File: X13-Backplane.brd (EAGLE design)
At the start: 86.4 x 139.3 mm, 36 parts, among them J1 PXC-PTSM-04-RA-1778641, J2 PXC-PTSM-04-RA-1778641, J3 PXC-8-RA-1778683, J4 PXC-PTSM-04-RA-1778641, J5 PXC-PTSM-04-RA-1778641, J8 PXC-8-RA-1778683

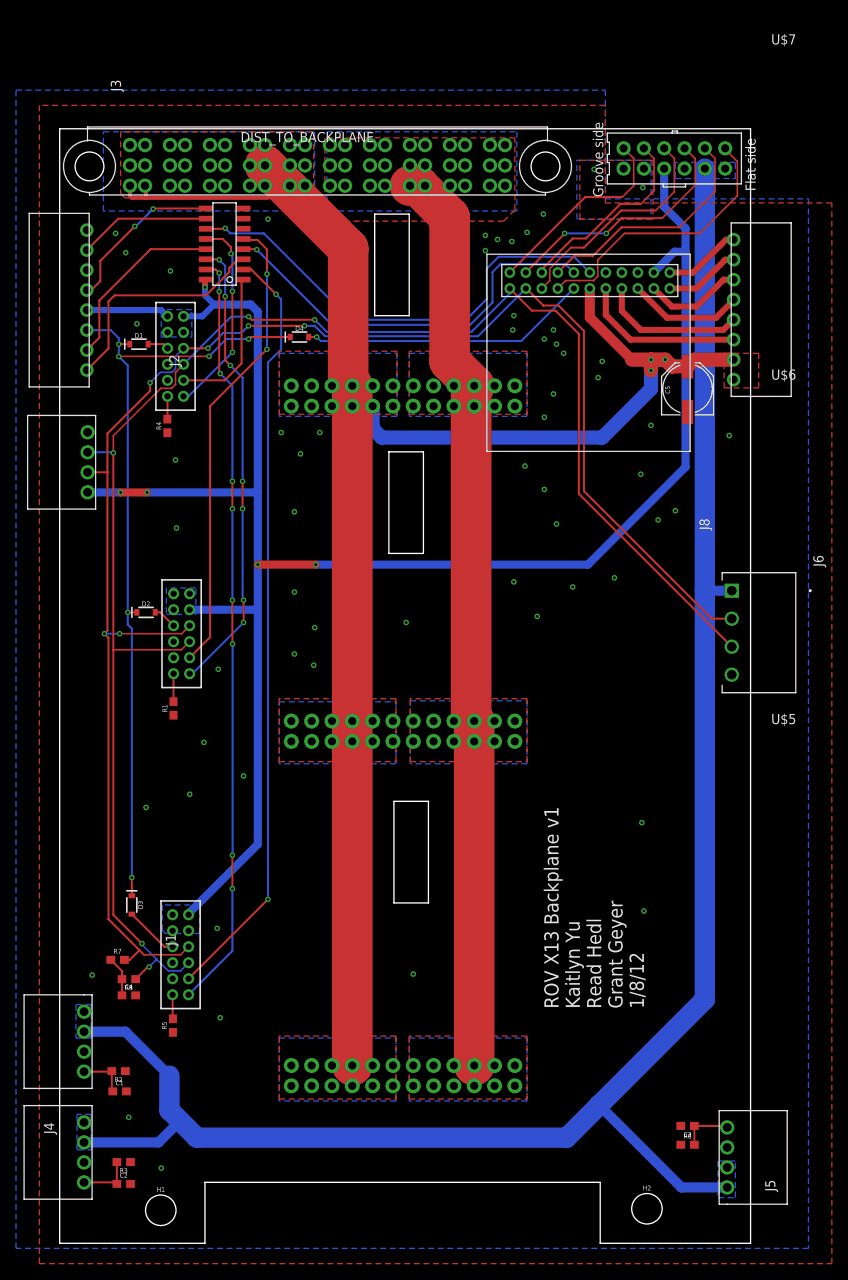
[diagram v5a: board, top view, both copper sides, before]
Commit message: OPE. GND connections were missing on esc controller connector
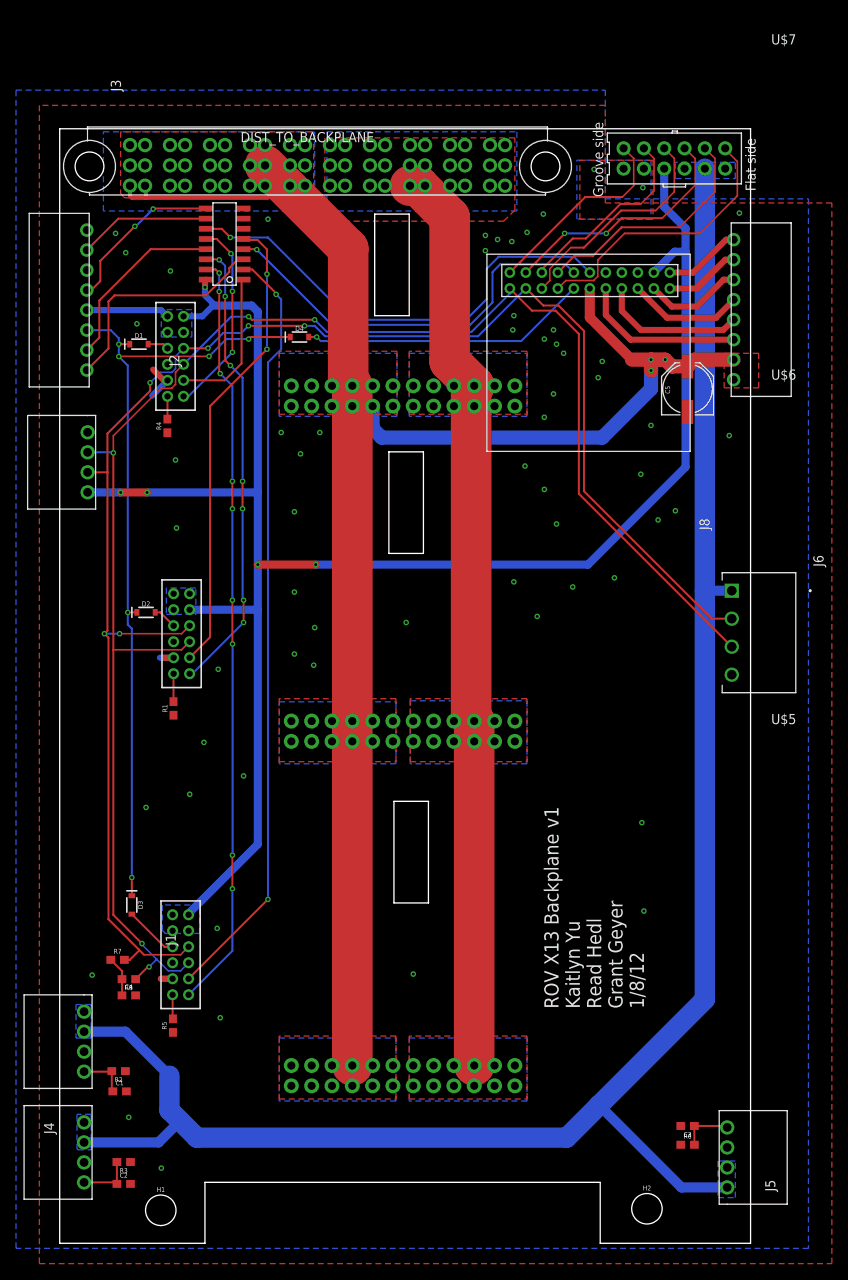
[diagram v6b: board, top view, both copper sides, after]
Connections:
- net GND: now also U$1.10, U$2.10, U$3.10
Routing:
- net GND: track 0.00 -> 10.8 mm, vias 59 -> 60
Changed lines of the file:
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@@
 <contactref element="MUX" pad="12"/>
 <contactref element="U$1" pad="11"/>
-<wire x1="25.89525" y1="125.5395" x2="28.0035" y2="125.5395" width="0.254" layer="1"/>
+<wire x1="25.89525" y1="125.5395" x2="27.2415" y2="125.5395" width="0.254" layer="1"/>
 <wire x1="29.02765" y1="123.698" x2="29.21" y2="123.51565" width="0.254" layer="16"/>
 <wire x1="29.21" y1="123.51565" x2="29.21" y2="118.999" width="0.254" layer="16"/>
@@
 <wire x1="29.21" y1="111.379" x2="23.702" y2="105.871" width="0.254" layer="16"/>
 <wire x1="23.702" y1="105.871" x2="23.098" y2="105.871" width="0.254" layer="16"/>
-<wire x1="28.0035" y1="125.5395" x2="29.02765" y2="124.51535" width="0.254" layer="1"/>
-<wire x1="29.02765" y1="124.51535" x2="29.02765" y2="123.698" width="0.254" layer="1"/>
+<wire x1="27.2415" y1="125.5395" x2="29.02765" y2="123.75335" width="0.254" layer="1"/>
+<wire x1="29.02765" y1="123.75335" x2="29.02765" y2="123.698" width="0.254" layer="1"/>
 <via x="29.02765" y="123.698" extent="1-16" drill="0.35"/>
 </signal>
@@
 <via x="39.37" y="72.263" extent="1-16" drill="0.35"/>
 <via x="30.607" y="58.42" extent="1-16" drill="0.35"/>
-<wire x1="30.57525" y1="126.8095" x2="21.463" y2="121.539" width="0" layer="19" extent="1-1"/>
+<contactref element="U$1" pad="10"/>
+<contactref element="U$2" pad="10"/>
+<contactref element="U$3" pad="10"/>
+<wire x1="21.098" y1="107.871" x2="20.653" y2="107.871" width="0.762" layer="1"/>
+<wire x1="20.653" y1="107.871" x2="19.304" y2="109.22" width="0.762" layer="1"/>
+<wire x1="21.098" y1="107.871" x2="19.177" y2="105.95" width="0.762" layer="16"/>
+<wire x1="21.86" y1="73.2" x2="20.145" y2="73.2" width="0.762" layer="16"/>
+<wire x1="21.86" y1="73.2" x2="20.622" y2="73.2" width="0.762" layer="1"/>
+<wire x1="21.733" y1="33.068" x2="20.241" y2="33.068" width="0.762" layer="1"/>
+<wire x1="21.733" y1="33.068" x2="20.399" y2="33.068" width="0.762" layer="16"/>
+<via x="92.583" y="128.778" extent="1-16" drill="0.35"/>
 </signal>
 <signal name="SWDIO_3">
 <contactref element="MUX" pad="2"/>
 <contactref element="U$3" pad="9"/>
-<wire x1="30.57525" y1="121.7295" x2="31.5595" y2="121.7295" width="0.254" layer="1"/>
+<wire x1="30.57525" y1="121.7295" x2="31.6865" y2="121.7295" width="0.254" layer="1"/>
 <via x="34.671" y="118.618" extent="1-16" drill="0.35"/>
 <wire x1="34.671" y1="118.618" x2="35.306" y2="117.983" width="0.254" layer="16"/>
 <wire x1="35.306" y1="117.983" x2="35.306" y2="111.76" width="0.254" layer="16"/>
-<wire x1="31.5595" y1="121.7295" x2="34.671" y2="118.618" width="0.254" layer="1"/>
+<wire x1="34.671" y1="118.745" x2="31.6865" y2="121.7295" width="0.254" layer="1"/>
+<wire x1="34.671" y1="118.745" x2="34.671" y2="118.618" width="0.254" layer="1"/>
 <wire x1="23.733" y1="33.068" x2="33.655" y2="42.99" width="0.254" layer="1"/>
 <wire x1="35.306" y1="111.76" x2="33.655" y2="110.109" width="0.254" layer="16"/>
@@
 <wire x1="20.32275" y1="116.64625" x2="21.098" y2="115.871" width="0.762" layer="16"/>
 <wire x1="32.385" y1="93.853" x2="32.385" y2="116.459" width="1.016" layer="16"/>
-<wire x1="32.385" y1="116.459" x2="31.496" y2="117.348" width="1.016" layer="16"/>
-<wire x1="31.496" y1="117.348" x2="26.924" y2="117.348" width="1.016" layer="16"/>
+<wire x1="32.385" y1="116.459" x2="31.623" y2="117.221" width="1.016" layer="16"/>
+<wire x1="31.623" y1="117.221" x2="26.797" y2="117.221" width="1.016" layer="16"/>
 <wire x1="26.924" y1="117.348" x2="25.781" y2="118.491" width="0.762" layer="16"/>
 <wire x1="25.781" y1="118.491" x2="25.781" y2="119.507" width="0.762" layer="16"/>
@@
 <wire x1="18.542" y1="93.853" x2="32.385" y2="93.853" width="1.016" layer="16"/>
 <wire x1="23.098" y1="115.871" x2="25.447" y2="115.871" width="0.762" layer="16"/>
-<wire x1="25.447" y1="115.871" x2="26.924" y2="117.348" width="0.762" layer="16"/>
+<wire x1="25.447" y1="115.871" x2="26.797" y2="117.221" width="0.762" layer="16"/>
+<wire x1="26.797" y1="117.221" x2="26.924" y2="117.348" width="0.762" layer="16"/>
 <via x="39.624" y="84.836" extent="1-16" drill="0.35"/>
 <wire x1="83.185" y1="134.33425" x2="83.185" y2="129.54" width="1.016" layer="16"/>
@@
 <wire x1="21.1772" y1="34.0678" x2="22.7328" y2="34.0678" width="0.2032" layer="16"/>
 <via x="14.3256" y="98.806" extent="1-16" drill="0.35"/>
-<wire x1="23.86" y1="75.2" x2="23.8346" y2="75.2" width="0.254" layer="1"/>
-<wire x1="23.8346" y1="75.2" x2="22.828" y2="74.1934" width="0.2032" layer="1"/>
 <via x="39.497" y="115.443" extent="1-16" drill="0.35"/>
 <wire x1="59.089" y1="113.919" x2="41.021" y2="113.919" width="0.254" layer="16"/>
@@
 <wire x1="72.517" y1="93.6905" x2="91.6305" y2="74.577" width="0.254" layer="1"/>
 <wire x1="14.3256" y1="98.806" x2="14.3256" y2="74.168" width="0.254" layer="1"/>
-<wire x1="14.351" y1="74.1934" x2="14.3256" y2="74.168" width="0.2032" layer="1"/>
-<wire x1="22.828" y1="74.1934" x2="14.351" y2="74.1934" width="0.2032" layer="1"/>
+<wire x1="14.3256" y1="74.168" x2="14.351" y2="74.1934" width="0.2032" layer="1"/>
 <contactref element="J2" pad="2"/>
 <wire x1="11.1125" y1="98.87775" x2="14.25385" y2="98.87775" width="0.254" layer="16"/>
 <wire x1="14.25385" y1="98.87775" x2="14.3256" y2="98.806" width="0.254" layer="16"/>
+<wire x1="22.8534" y1="74.1934" x2="23.86" y2="75.2" width="0.2032" layer="1"/>
+<wire x1="14.351" y1="74.1934" x2="22.8534" y2="74.1934" width="0.2032" layer="1"/>
 </signal>
 <signal name="5V">
@@
 <contactref element="MUX" pad="11"/>
 <contactref element="U$4" pad="12"/>
-<wire x1="25.89525" y1="126.8095" x2="28.2575" y2="126.8095" width="0.254" layer="1"/>
-<wire x1="28.2575" y1="126.8095" x2="28.321" y2="126.873" width="0.254" layer="1"/>
-<via x="28.321" y="126.873" extent="1-16" drill="0.35"/>
-<wire x1="28.321" y1="126.873" x2="28.956" y2="126.238" width="0.254" layer="16"/>
-<wire x1="28.956" y1="126.238" x2="33.147" y2="126.238" width="0.254" layer="16"/>
+<wire x1="33.655" y1="125.73" x2="28.956" y2="125.73" width="0.254" layer="16"/>
 <wire x1="73.8835" y1="121.3485" x2="71.915" y2="123.317" width="0.254" layer="16"/>
 <wire x1="71.915" y1="123.317" x2="62.484" y2="123.317" width="0.254" layer="16"/>
 <wire x1="43.942" y1="115.443" x2="58.42" y2="115.443" width="0.254" layer="16"/>
 <wire x1="58.42" y1="115.443" x2="61.008" y2="118.031" width="0.254" layer="16"/>
-<wire x1="33.147" y1="126.238" x2="43.942" y2="115.443" width="0.254" layer="16"/>
+<wire x1="33.655" y1="125.73" x2="43.942" y2="115.443" width="0.254" layer="16"/>
 <wire x1="61.008" y1="121.841" x2="62.484" y2="123.317" width="0.254" layer="16"/>
 <wire x1="61.008" y1="118.031" x2="61.008" y2="121.841" width="0.254" layer="16"/>
+<via x="28.956" y="125.73" extent="1-16" drill="0.35"/>
+<wire x1="28.956" y1="125.73" x2="27.8765" y2="126.8095" width="0.254" layer="1"/>
+<wire x1="27.8765" y1="126.8095" x2="25.89525" y2="126.8095" width="0.254" layer="1"/>
 </signal>
 </signals>

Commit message: integration
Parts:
- moved C5 8.17 mm to (90.6, 99.9)
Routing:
- net 12V: track 209.1 -> 206.1 mm
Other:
- outline, holes or cut-outs redrawn
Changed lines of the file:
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@@
 Grant Geyer
 1/8/12</text>
-<wire x1="48.768" y1="86.233" x2="48.768" y2="98.933" width="0" layer="20"/>
-<wire x1="48.768" y1="98.933" x2="53.086" y2="98.933" width="0" layer="20"/>
-<wire x1="53.086" y1="98.933" x2="53.086" y2="86.233" width="0" layer="20"/>
-<wire x1="53.086" y1="86.233" x2="48.768" y2="86.233" width="0" layer="20"/>
-<wire x1="49.403" y1="42.545" x2="49.403" y2="55.245" width="0" layer="20"/>
-<wire x1="49.403" y1="55.245" x2="53.721" y2="55.245" width="0" layer="20"/>
-<wire x1="53.721" y1="55.245" x2="53.721" y2="42.545" width="0" layer="20"/>
-<wire x1="53.721" y1="42.545" x2="49.403" y2="42.545" width="0" layer="20"/>
+<wire x1="47.752" y1="86.36" x2="47.752" y2="100.457" width="0" layer="20"/>
+<wire x1="47.752" y1="100.457" x2="54.102" y2="100.457" width="0" layer="20"/>
+<wire x1="54.102" y1="100.457" x2="54.102" y2="86.36" width="0" layer="20"/>
+<wire x1="54.102" y1="86.36" x2="47.752" y2="86.36" width="0" layer="20"/>
+<wire x1="48.133" y1="42.545" x2="48.133" y2="57.15" width="0" layer="20"/>
+<wire x1="48.133" y1="57.15" x2="54.864" y2="57.15" width="0" layer="20"/>
+<wire x1="54.864" y1="57.15" x2="54.864" y2="42.545" width="0" layer="20"/>
+<wire x1="54.864" y1="42.545" x2="48.133" y2="42.545" width="0" layer="20"/>
 <wire x1="46.99" y1="115.951" x2="46.99" y2="128.651" width="0" layer="20"/>
 <wire x1="46.99" y1="128.651" x2="51.308" y2="128.651" width="0" layer="20"/>
-<wire x1="51.308" y1="128.651" x2="51.308" y2="115.951" width="0" layer="20"/>
-<wire x1="51.308" y1="115.951" x2="46.99" y2="115.951" width="0" layer="20"/>
+<wire x1="51.308" y1="128.651" x2="51.308" y2="126.365" width="0" layer="20"/>
+<wire x1="51.308" y1="126.365" x2="52.451" y2="125.222" width="0" layer="20"/>
+<wire x1="52.451" y1="125.222" x2="52.451" y2="115.951" width="0" layer="20"/>
+<wire x1="52.451" y1="115.951" x2="46.99" y2="115.951" width="0" layer="20"/>
 <polygon width="0.1524" layer="29">
 <vertex x="41.529" y="17.526"/>
@@
 <attribute name="VALUE" x="37.592" y="112.522" size="0.6096" layer="27" font="vector" ratio="20" align="top-center"/>
 </element>
-<element name="C5" library="Panasonic 47 uF cap - EEE-1CA470SP" package="PANASONIC_D" package3d_urn="urn:adsk.eagle:package:24384400/2" value="47uF" x="86.106" y="106.807" smashed="yes" rot="R90">
-<attribute name="NAME" x="83.312" y="106.68" size="0.6096" layer="25" font="vector" ratio="20" rot="R270" align="bottom-center"/>
-<attribute name="PROD_ID" value="CAP-08478" x="86.106" y="106.807" size="1.778" layer="27" rot="R90" display="off"/>
-<attribute name="VALUE" x="88.9" y="106.807" size="0.6096" layer="27" font="vector" ratio="20" rot="R270" align="top-center"/>
+<element name="C5" library="Panasonic 47 uF cap - EEE-1CA470SP" package="PANASONIC_D" package3d_urn="urn:adsk.eagle:package:24384400/2" value="47uF" x="90.551" y="99.949" smashed="yes" rot="R90">
+<attribute name="NAME" x="87.757" y="99.822" size="0.6096" layer="25" font="vector" ratio="20" rot="R270" align="bottom-center"/>
+<attribute name="PROD_ID" value="CAP-08478" x="90.551" y="99.949" size="1.778" layer="27" rot="R90" display="off"/>
+<attribute name="VALUE" x="93.345" y="99.949" size="0.6096" layer="27" font="vector" ratio="20" rot="R270" align="top-center"/>
 </element>
 </elements>
@@
 <via x="68.199" y="103.251" extent="1-16" drill="0.35"/>
 <via x="81.534" y="102.235" extent="1-16" drill="0.35"/>
-<via x="91.313" y="100.965" extent="1-16" drill="0.35"/>
+<via x="92.075" y="94.107" extent="1-16" drill="0.35"/>
 <via x="16.256" y="15.748" extent="1-16" drill="0.35"/>
 <via x="20.32" y="9.398" extent="1-16" drill="0.35"/>
@@
 <wire x1="21.733" y1="33.068" x2="20.399" y2="33.068" width="0.762" layer="16"/>
 <via x="92.583" y="128.778" extent="1-16" drill="0.35"/>
+<wire x1="92.075" y1="94.107" x2="90.551" y2="97.049" width="0" layer="19" extent="1-1"/>
 </signal>
 <signal name="SWDIO_3">
@@
 <vertex x="35.052" y="25.654"/>
 </polygon>
-<polygon width="1.27" layer="1">
-<vertex x="90.678" y="111.252"/>
-<vertex x="90.678" y="106.934"/>
-<vertex x="94.996" y="106.934"/>
+<polygon width="1.016" layer="1">
+<vertex x="89.027" y="111.252"/>
+<vertex x="89.027" y="100.076"/>
+<vertex x="94.996" y="100.076"/>
 <vertex x="94.996" y="111.252"/>
 </polygon>
@@
 <wire x1="73.8835" y1="115.72435" x2="73.8835" y2="119.3485" width="1.27" layer="1"/>
 <wire x1="46.736" y1="104.648" x2="46.736" y2="101.854" width="1.778" layer="16"/>
-<wire x1="46.736" y1="101.854" x2="47.879" y2="100.711" width="1.778" layer="16"/>
 <wire x1="81.534" y1="106.807" x2="81.534" y2="109.093" width="1.778" layer="16"/>
-<wire x1="81.534" y1="106.807" x2="75.438" y2="100.711" width="1.778" layer="16"/>
+<wire x1="81.534" y1="106.807" x2="76.581" y2="101.854" width="1.778" layer="16"/>
 <via x="81.534" y="109.093" extent="1-16" drill="0.35"/>
-<wire x1="47.879" y1="100.711" x2="75.438" y2="100.711" width="1.778" layer="16"/>
+<wire x1="46.736" y1="101.854" x2="76.581" y2="101.854" width="1.778" layer="16"/>
 <wire x1="81.534" y1="109.093" x2="81.534" y2="110.4545" width="1.778" layer="16"/>
 <via x="81.534" y="110.4545" extent="1-16" drill="0.35"/>
 <wire x1="81.534" y1="110.4545" x2="83.312" y2="110.4545" width="1.778" layer="16"/>
 <via x="83.312" y="110.4545" extent="1-16" drill="0.35"/>
-<wire x1="91.86" y1="110.4545" x2="86.9535" y2="110.4545" width="1.778" layer="1"/>
-<wire x1="86.9535" y1="110.4545" x2="86.106" y2="109.607" width="1.778" layer="1"/>
-<wire x1="86.106" y1="109.607" x2="84.1595" y2="109.607" width="1.778" layer="1"/>
-<wire x1="84.1595" y1="109.607" x2="83.312" y2="110.4545" width="1.778" layer="1"/>
+<wire x1="90.551" y1="110.4545" x2="83.312" y2="110.4545" width="1.778" layer="1"/>
 <wire x1="83.312" y1="110.4545" x2="81.534" y2="110.4545" width="1.778" layer="1"/>
 <wire x1="81.534" y1="110.4545" x2="79.15335" y2="110.4545" width="1.778" layer="1"/>
